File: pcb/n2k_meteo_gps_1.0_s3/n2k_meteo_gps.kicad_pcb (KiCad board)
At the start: 2 copper layers, 55 x 54.5 mm, 33 parts, among them J10 3.3-5V, U1 LM7805_TO220, U3 MCP2562-E-P, U4 PC817, U5 ESP32-C3_SUPERMINI, U6 PC817

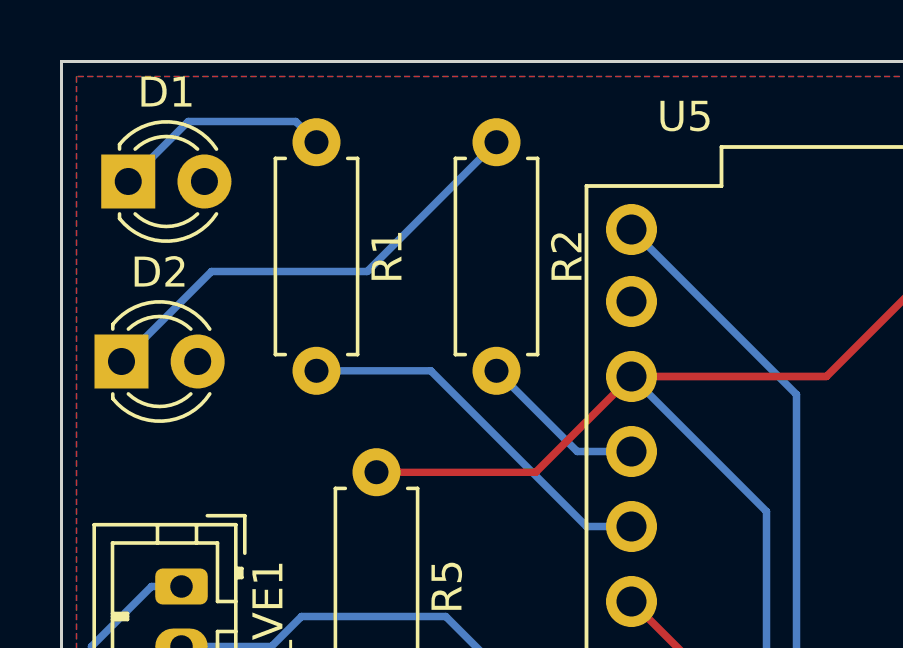
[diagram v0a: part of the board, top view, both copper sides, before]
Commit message: Fixed problem with gps i2c that was disable in loop
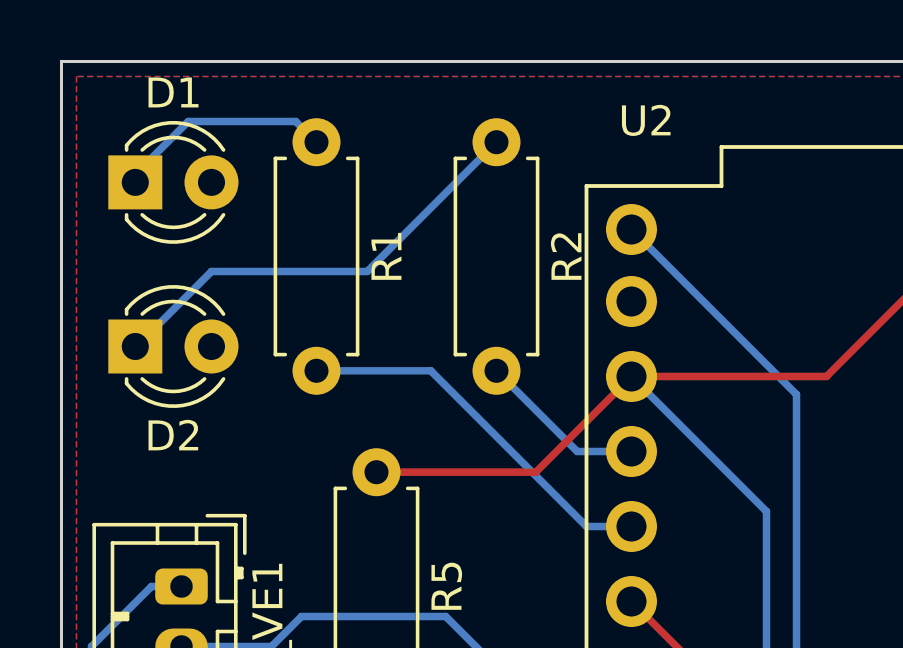
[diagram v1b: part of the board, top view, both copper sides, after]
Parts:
- removed U5: ESP32-C3_SUPERMINI, Library:WAVESHARE_DEVKIT_ESP32-C3-ZERO
- added U2: ESP32-S3_SUPERMINI, Library:WAVESHARE_DEVKIT_ESP32-S3-ZERO, F.Cu at (45.5, 56.2)
- R11: value 4.7K -> 4K7
- R5: value 4.7KΩ -> 2K2
- R8: value 4.7K -> 2K2
- moved D2 0.68 mm to (21.5, 50.2)
- moved D1 0.24 mm to (21.5, 44.8)

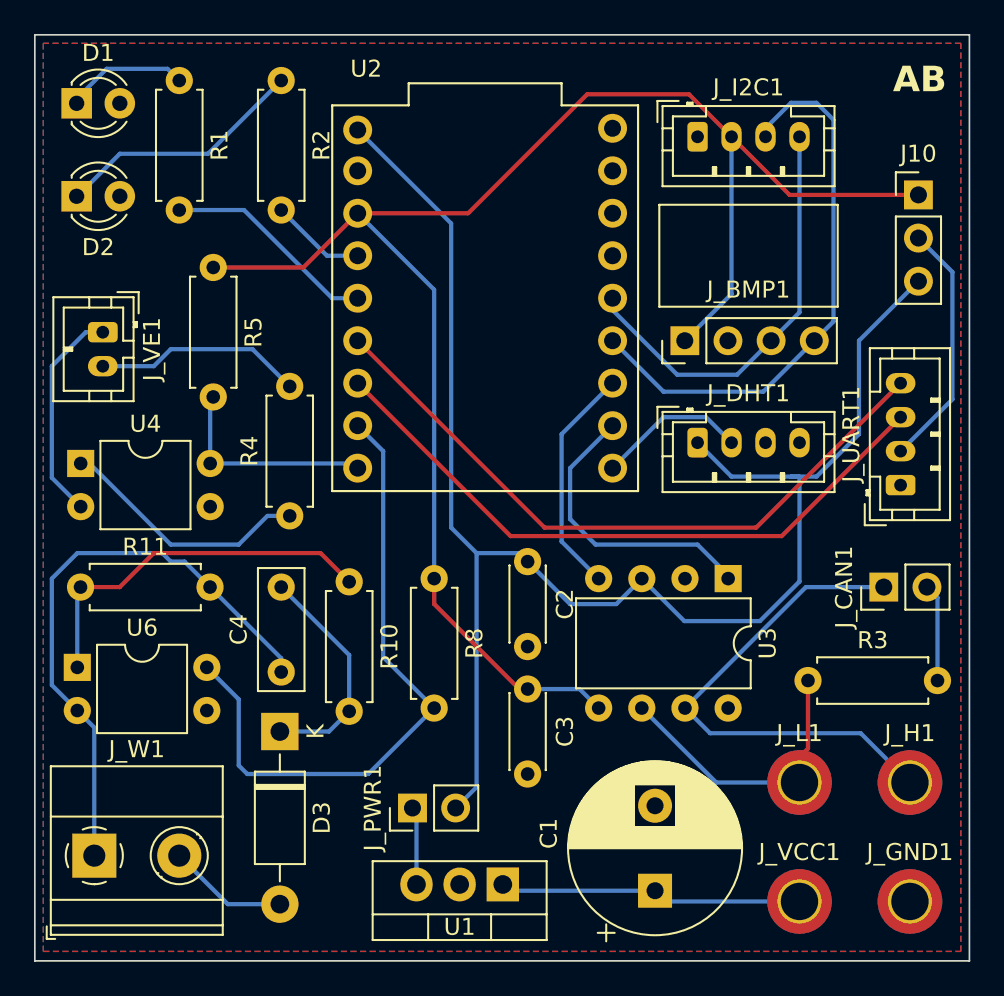
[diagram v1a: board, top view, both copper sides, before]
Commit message: PCB - added xiao seeed studio
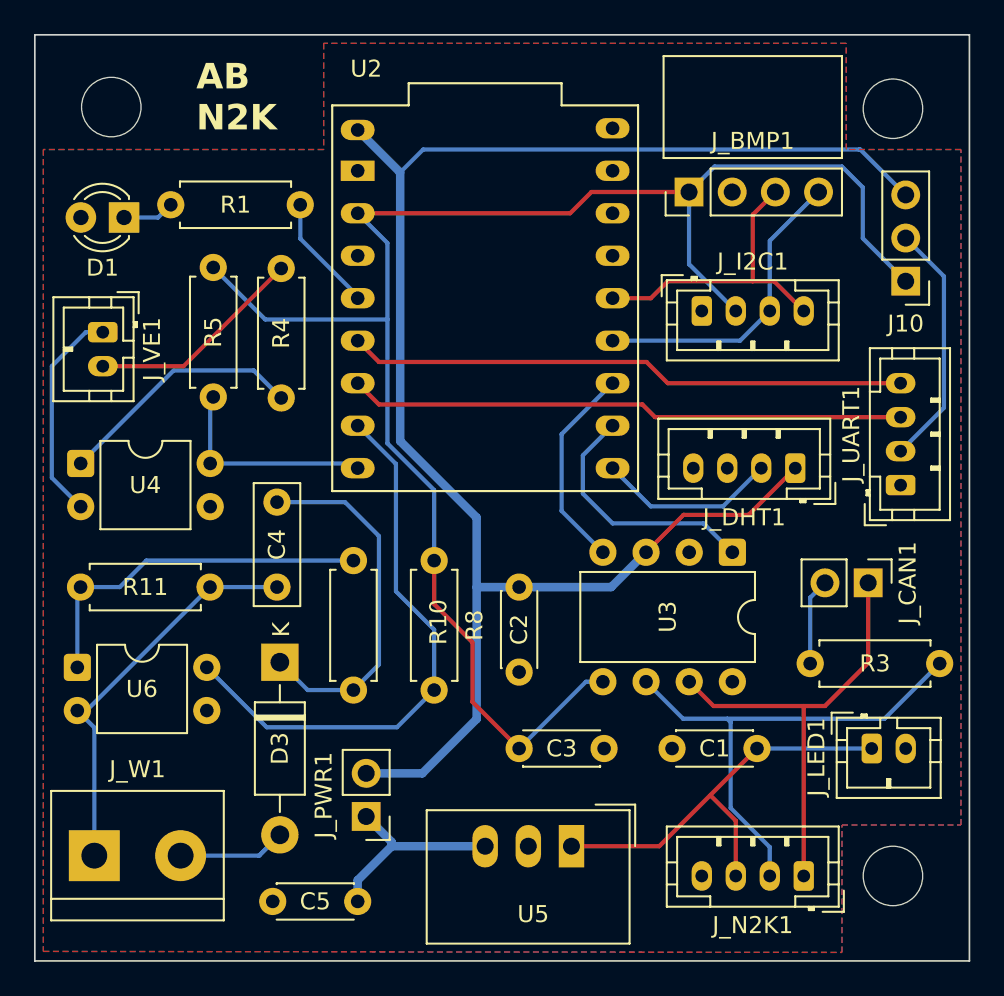
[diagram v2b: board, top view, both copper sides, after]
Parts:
- removed D2: LED, LED_THT:LED_D3.0mm
- removed J_GND1: CAN GND, MountingHole:MountingHole_2.2mm_M2_DIN965_Pad_TopBottom
- removed J_H1: CAN H, MountingHole:MountingHole_2.2mm_M2_DIN965_Pad_TopBottom
- removed J_L1: CAN L, MountingHole:MountingHole_2.2mm_M2_DIN965_Pad_TopBottom
- removed J_VCC1: CAN 12V, MountingHole:MountingHole_2.2mm_M2_DIN965_Pad_TopBottom
- removed R2: 100Ω, Resistor_THT:R_Axial_DIN0207_L6.3mm_D2.5mm_P7.62mm_Horizontal
- removed U1: LM7805_TO220, Package_TO_SOT_THT:TO-220-3_Vertical
- added C5: 10uF, Capacitor_THT:C_Disc_D4.3mm_W1.9mm_P5.00mm, F.Cu at (38.0, 91.8)
- added J_LED1: PWR_LED, Connector_JST:JST_PH_B2B-PH-K_1x02_P2.00mm_Vertical, F.Cu at (68.3, 82.8)
- added J_N2K1: NMEA2000, Connector_JST:JST_PH_B4B-PH-K_1x04_P2.00mm_Vertical, F.Cu at (64.3, 90.2)
- added U5: TSR_1-2450, Converter_DCDC:Converter_DCDC_TRACO_TSR-1_THT, F.Cu at (50.6, 88.5)
- C1: value 100uF -> 10uF; footprint Capacitor_THT:CP_Radial_D10.0mm_P5.00mm -> Capacitor_THT:C_Disc_D4.3mm_W1.9mm_P5.00mm
- J_W1: footprint TerminalBlock_Phoenix:TerminalBlock_Phoenix_MKDS-1,5-2_1x02_P5.00mm_Horizontal -> TerminalBlock:TerminalBlock_bornier-2_P5.08mm
- U2: footprint Library:WAVESHARE_DEVKIT_ESP32-S3-ZERO -> MyLib:WAVESHARE_DEVKIT_ESP32-S3-ZERO
- moved C1 10.3 mm to (61.5, 82.8), turned to 180 degrees
- moved J_I2C1 10.3 mm to (58.3, 57.0)
- moved J_BMP1 8.75 mm to (57.5, 50.0)
- moved R3 7.81 mm to (72.3, 77.8), turned to 180 degrees
- moved R1 7.33 mm to (27.1, 50.8), turned to 0 degrees
- moved D1 7.28 mm to (24.3, 51.5), turned to 180 degrees
- moved R4 6.96 mm to (33.5, 62.1)
- moved J_DHT1 5.94 mm to (63.8, 66.2), turned to 180 degrees
- moved J10 5.14 mm to (70.3, 55.2), turned to 180 degrees
- moved C4 5.01 mm to (33.3, 73.2)
- moved D3 4.08 mm to (33.5, 77.7)
- moved C3 3.54 mm to (47.5, 82.8), turned to 0 degrees
- moved J_PWR1 2.77 mm to (38.5, 86.8), turned to 180 degrees
- moved C2 1.58 mm to (47.5, 73.2)
- moved U3 1.57 mm to (60.1, 71.2)
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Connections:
- U2 pad 1: Net-(U2-GPIO1) -> unconnected-(U2-GPIO1-Pad1)
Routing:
- net Net-(D2-K): track 15.5 -> 0.00 mm
- net Net-(J_BMP1-Pin_4): track 33.4 -> 18.2 mm
- net Net-(J_N2K1-Pin_2): track 17.3 -> 29.8 mm
- net Net-(J_W1-Pin_1): track 34.8 -> 23.7 mm
- net Net-(D3-K): track 13.5 -> 21.5 mm
- net +12V: track 17.9 -> 25.4 mm
- net Net-(J_PWR1-Pin_1): track 4.60 -> 11.9 mm
- net Net-(J_UART1-Pin_4): track 40.0 -> 33.0 mm
- net Net-(J_BMP1-Pin_3): track 25.1 -> 18.2 mm
- net Net-(J_UART1-Pin_3): track 38.6 -> 32.8 mm
- net Net-(U2-GPIO2): track 12.6 -> 6.90 mm
- net Net-(U2-GPIO1): track 5.61 -> 0.00 mm
- net Net-(U2-GPIO5): track 38.4 -> 33.2 mm
- net Net-(D1-K): track 7.39 -> 3.06 mm
- net +5V: track 94.7 -> 98.4 mm
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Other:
- outline, holes or cut-outs redrawn
- board text added: "AB N2K"
- board text removed: "AB"

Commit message: PCB
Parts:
- removed C5: 10uF, Capacitor_THT:C_Disc_D4.3mm_W1.9mm_P5.00mm
- removed J_LED1: PWR_LED, Connector_JST:JST_PH_B2B-PH-K_1x02_P2.00mm_Vertical
- removed J_N2K1: NMEA2000, Connector_JST:JST_PH_B4B-PH-K_1x04_P2.00mm_Vertical
- removed U5: TSR_1-2450, Converter_DCDC:Converter_DCDC_TRACO_TSR-1_THT
- added D2: LED, LED_THT:LED_D3.0mm, F.Cu at (21.1, 50.8)
- added J_GND1: CAN GND, MountingHole:MountingHole_2.2mm_M2_DIN965_Pad_TopBottom, F.Cu at (70.5, 91.8)
- added J_H1: CAN H, MountingHole:MountingHole_2.2mm_M2_DIN965_Pad_TopBottom, F.Cu at (70.5, 84.8)
- added J_L1: CAN L, MountingHole:MountingHole_2.2mm_M2_DIN965_Pad_TopBottom, F.Cu at (64.0, 84.8)
- added J_VCC1: CAN 12V, MountingHole:MountingHole_2.2mm_M2_DIN965_Pad_TopBottom, F.Cu at (64.0, 91.8)
- added R2: 100Ω, Resistor_THT:R_Axial_DIN0207_L6.3mm_D2.5mm_P7.62mm_Horizontal, F.Cu at (33.5, 43.4)
- added U1: LM7805_TO220, Package_TO_SOT_THT:TO-220-3_Vertical, F.Cu at (46.6, 90.8)
- C1: value 10uF -> 100uF; footprint Capacitor_THT:C_Disc_D4.3mm_W1.9mm_P5.00mm -> Capacitor_THT:CP_Radial_D10.0mm_P5.00mm
- J_W1: footprint TerminalBlock:TerminalBlock_bornier-2_P5.08mm -> TerminalBlock_Phoenix:TerminalBlock_Phoenix_MKDS-1,5-2_1x02_P5.00mm_Horizontal
- moved C1 10.3 mm to (55.5, 91.1), turned to 90 degrees
- moved J_I2C1 10.3 mm to (58.0, 46.8)
- moved J_BMP1 8.75 mm to (57.3, 58.8)
- moved R3 7.81 mm to (64.5, 78.8), turned to 0 degrees
- moved D1 7.40 mm to (21.3, 44.8), turned to 0 degrees
- moved R1 7.33 mm to (27.6, 43.4), turned to -90 degrees
- moved R4 6.96 mm to (34.0, 69.1)
- moved J_DHT1 5.94 mm to (58.0, 64.8), turned to 0 degrees
- moved J10 5.14 mm to (71.0, 50.2), turned to 0 degrees
- moved C4 5.01 mm to (33.5, 78.2)
- moved D3 4.08 mm to (33.5, 81.8)
- moved C3 3.54 mm to (48.0, 79.2), turned to -90 degrees
- moved J_PWR1 2.77 mm to (41.3, 86.2), turned to 90 degrees
- moved C2 1.58 mm to (48.0, 71.8)
- moved U3 1.57 mm to (59.9, 72.8)
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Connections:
- U2 pad 1: unconnected-(U2-GPIO1-Pad1) -> Net-(U2-GPIO1)
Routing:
- net Net-(D2-K): track 0.00 -> 15.5 mm
- net Net-(J_BMP1-Pin_4): track 18.2 -> 33.4 mm
- net Net-(J_L1-Pin_1): track 29.8 -> 17.3 mm
- net Net-(J_W1-Pin_1): track 23.7 -> 34.8 mm
- net Net-(D3-K): track 21.5 -> 13.5 mm
- net +12V: track 25.4 -> 17.9 mm
- net Net-(J_PWR1-Pin_1): track 11.9 -> 4.60 mm
- net Net-(J_UART1-Pin_4): track 33.0 -> 40.0 mm
- net Net-(J_BMP1-Pin_3): track 18.2 -> 25.1 mm
- net Net-(J_UART1-Pin_3): track 32.8 -> 38.6 mm
- net Net-(U2-GPIO2): track 6.90 -> 12.6 mm
- net Net-(U2-GPIO1): track 0.00 -> 5.61 mm
- net Net-(U2-GPIO5): track 33.2 -> 38.4 mm
- net Net-(D1-K): track 3.06 -> 7.39 mm
- net +5V: track 98.4 -> 94.7 mm
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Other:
- outline, holes or cut-outs redrawn
- board text added: "AB"
- board text removed: "AB N2K"
